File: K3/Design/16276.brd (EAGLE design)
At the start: 40.6 x 52.1 mm, 75 parts, among them J1 PST1,0/4-3,5, J3 PBC03SAA, Q1 K1N, Q10 DMB, Q11 34N, Q12 34N, Q13 K1N, Q14 K1N, Q15 K1N, Q16 K38, Q17 K38, Q18 DMB, Q19 K3N, Q2 DMB, Q20 K3N, Q21 K1N, Q22 DMB, Q23 34N, Q24 K84, Q3 34N, Q4 DMB, Q5 K3N, Q6 K1N, Q7 K1N, Q8 K1N, Q9 K1N, U1 MC34063A, U2 74HC238

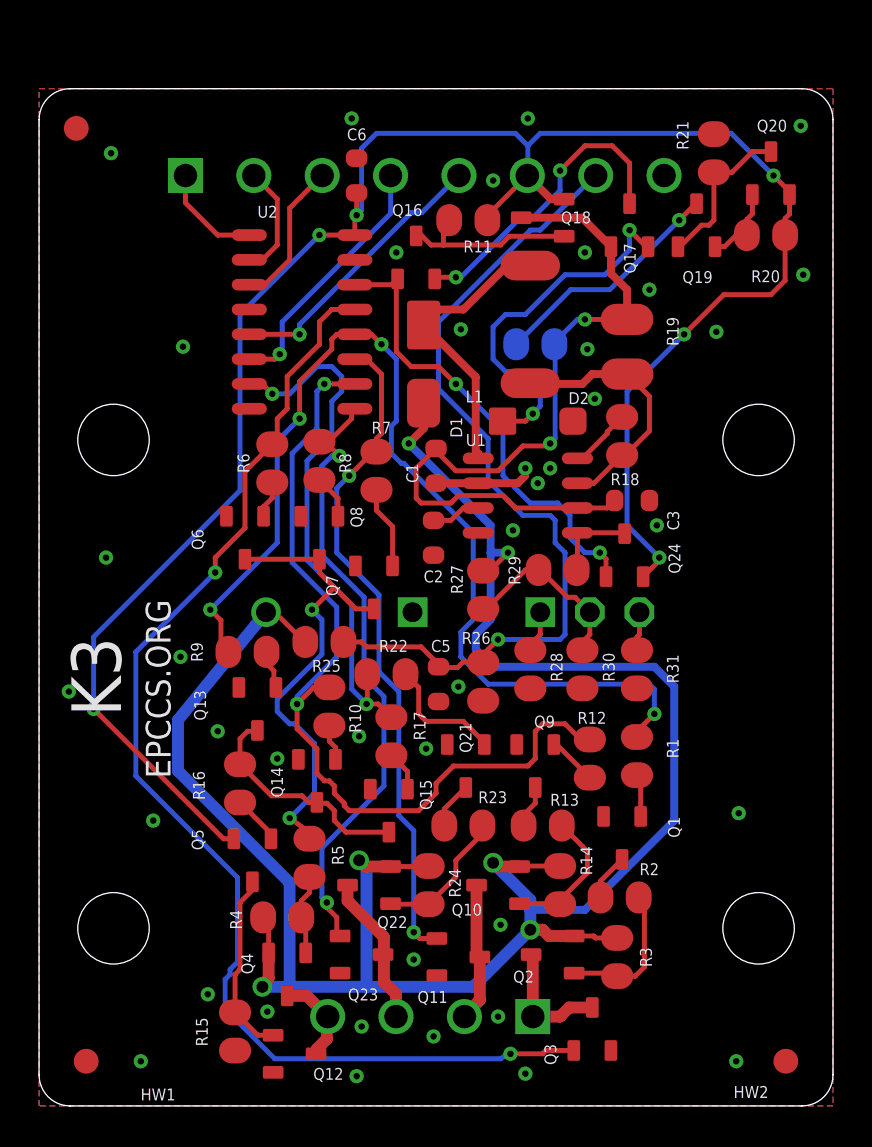
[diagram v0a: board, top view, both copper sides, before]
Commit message: K3: use E3 input to turn on curr source
that test for bridge shorts
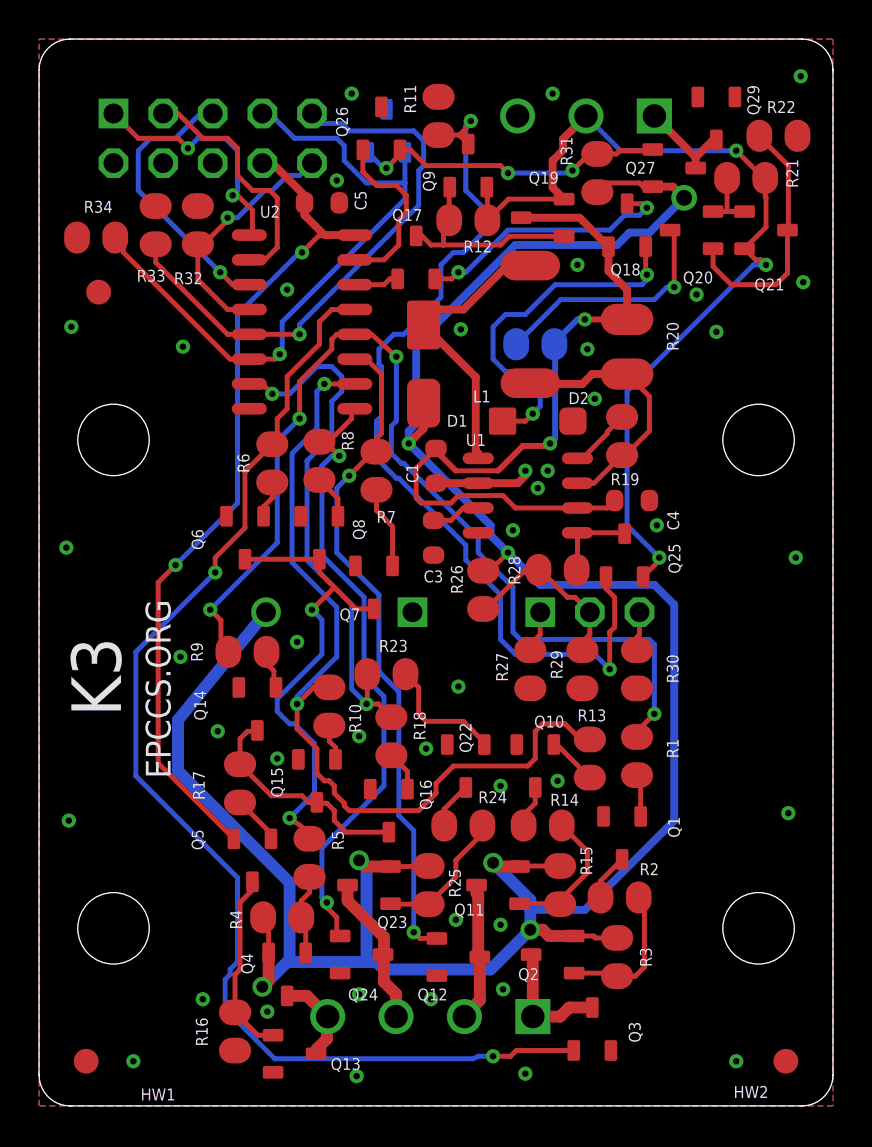
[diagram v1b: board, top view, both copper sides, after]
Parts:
- removed C6: .1uF, C-C:C0603(1608)
- added J4: PBC03SAA, J-HDR2.54mm:1X3
- added Q25: K84, Q-PCH:SOT23
- added Q26: K38, Q-NCH:SOT23
- added Q27: DMB, Q-PCH:SOT23
- added Q28: OPEN, Q-NCH:SOT23
- added Q29: K1N, Q-NPN:SOT23
- added R32, R33, R34: 10K, R-C:C0805(2012)
- added TP1: TPPAD1-08, J-TP:P1-08
- C2: value 330pF -> 2200uF; device C-C:C0603(1608) -> C-Al:E7,5-18
- C3: value .1uF -> 330pF
- C4: value 2200uF -> .1uF; device C-Al:E7,5-18 -> C-C:C0603(1608)
- C5: value .01uF -> .1uF
- J2: value (none) -> PST1,0&3-3,5; device J-HDR3.5mm:MCV8 -> J-HDR3.5mm:MCV3
- J3: value PBC03SAA -> (none); device J-HDR2.54mm:1X3 -> J-HDR2.54mm:2X5
- Q10, Q22: value DMB -> K1N; device Q-PCH:SOT23 -> Q-NPN:SOT23
- Q11, Q23: value 34N -> DMB; device Q-NCH:SOT23 -> Q-PCH:SOT23
- Q13: value K1N -> 34N; device Q-NPN:SOT23 -> Q-NCH:SOT23
- Q16: value K38 -> K1N; device Q-NCH:SOT23 -> Q-NPN:SOT23
- Q18: value DMB -> K38; device Q-PCH:SOT23 -> Q-NCH:SOT23
- Q19: value K3N -> DMB; device Q-PNP:SOT23 -> Q-PCH:SOT23
- Q21: value K1N -> K3N; device Q-NPN:SOT23 -> Q-PNP:SOT23
- Q24: value K84 -> 34N; device Q-PCH:SOT23 -> Q-NCH:SOT23
- Q9: value K1N -> K84; device Q-NPN:SOT23 -> Q-PCH:SOT23
- R11, R22: value 10K -> 49.9k
- R13, R16, R23: value 100K -> 10K
- R15: value 10K -> 100K
- R18: value 182 -> 100K
- R19: value 1 -> 182; device R-C:C1210(3225) -> R-C:C0805(2012)
- R20: value 32.4 -> 1; device R-C:C0805(2012) -> R-C:C1210(3225)
- R21: value 49.9k -> 32.4
- R26: value 5.62K -> 100K
- R27: value 100K -> 15.8k
- R28: value 15.8k -> 10K
- R29: value 10K -> 8.45k
- R30: value 8.45k -> 43.2k
- R31: value 43.2k -> 100K
- moved R22 34.1 mm to (37.8, 49.7), turned to 180 degrees
- moved J3 33.6 mm to (3.81, 50.8)
- moved Q21 31.4 mm to (37.2, 44.8), turned to 270 degrees
- moved Q9 30.9 mm to (22.0, 48.1), turned to 0 degrees
- moved Q16 28.4 mm to (17.9, 15.1), turned to 180 degrees
- moved R12 28.3 mm to (22.0, 45.3), turned to 180 degrees
- moved R31 25.5 mm to (28.6, 47.8), turned to 90 degrees
- moved C5 25.4 mm to (14.5, 46.2), turned to 0 degrees
- moved Q24 24.5 mm to (16.5, 7.75), turned to 270 degrees
- moved J2 24.2 mm to (31.5, 50.7), turned to 0 degrees
- moved R18 19.4 mm to (18.0, 18.9), turned to 270 degrees
- moved R15 18.2 mm to (26.7, 11.3)
- moved Q13 17.8 mm to (13.1, 2.67), turned to 270 degrees
- moved C4 16.0 mm to (30.4, 31.0), flipped to the top, turned to 0 degrees
- moved R25 13.5 mm to (19.9, 11.3), turned to 90 degrees
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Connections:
- removed net !EN: J2.5, U2.5
- removed net +5V: C6.1, J2.6, Q18.2(S), Q20.E, Q24.2(S), Q5.E, R11.1, R20.2, U2.16
- removed net 5.3%BOOST: C5.1, J2.7, R25.2, R26.2
- removed net EN: J2.4, U2.6
- new net !E1: J3.10, R32.1, U2.4
- new net !E2: J3.9, R33.1, U2.5
- new net DISCHARGE: J2.1, Q27.3(D), Q29.C
- new net E3: J3.7, Q28.1(G), R34.1, U2.6
- new net FEED: C1.1, C4.1, D3.K, Q18.1(G), Q19.3(D), R20.1, U1.6
- new net N$10: Q26.2(S), Q27.1(G), Q28.2(S), R31.2
- new net N$11: Q26.1(G), U2.15
- new net N$2: Q25.1(G), Q9.3(D), R11.1
- new net SUPPLY: J2.2, Q19.2(S), Q21.E, Q25.2(S), Q9.2(S), R12.1, R21.2
- net 0V: now also C2.-, C4.2, J2.3, J3.2, J3.4, J3.6, Q10.E, Q13.2(S), Q16.E, Q22.E, Q24.2(S), Q26.3(D), Q28.3(D), Q29.B, Q29.E, R11.2, R16.1, R22.1, R27.1, R29.2, R32.2, R33.2, R34.2; no longer C2.2, C4.-, C6.2, J2.8, Q11.2(S), Q13.E, Q21.E, Q23.2(S), Q9.E, R15.1, R21.1, R26.1, R28.1, R31.2, U2.4
- net A0: now also J3.1; no longer J2.1
- net A1: now also J3.3; no longer J2.2
- net A2: now also J3.5; no longer J2.3
- net BOOST: now also C2.+, Q11.2(S), Q23.2(S), Q27.2(S), R15.2, R25.2, R26.1, R31.1, TP1.TP; no longer C4.+, Q10.2(S), Q22.2(S), R14.2, R24.2, R25.1, R27.1
- net COM: now also Q13.3(D); no longer Q12.3(D)
- net K2: now also Q12.3(D); no longer Q10.3(D)
- net K3: now also Q24.3(D); no longer Q22.3(D)
- net N$120: now also J4.3, R30.1; no longer J3.3, R31.1
- net N$121: now also J4.1, R29.1; no longer J3.1, R30.1
- net N$128: now also Q20.E, Q21.B, R21.1; no longer Q19.E, Q20.B, R20.1
- net N$13: now also R19.2; no longer R18.2
- net N$132: now also Q20.B, Q21.C, R22.2; no longer Q19.B, Q20.C, R21.2
- net N$14: now also R19.1, R20.2; no longer R18.1, R19.2
- net N$16: now also C3.1; no longer C2.1
- net N$21: now also Q13.1(G), R16.2; no longer Q12.1(G), R15.2
- net N$22: now also Q17.3(D), Q19.1(G), Q9.1(G), R12.2; no longer Q16.3(D), Q18.1(G), R11.2
- net N$26: now also J4.2, R26.2, R28.1; no longer J3.2, R28.2, R29.1
- net N$3: now also Q23.1(G), R24.2, R25.1; no longer Q22.1(G), R23.2, R24.1
- net N$4: now also Q22.C, R24.1; no longer Q21.C, R23.1
- net N$43: now also Q11.1(G), R14.2, R15.1; no longer Q10.1(G), R13.2, R14.1
- net N$44: now also Q10.C, R14.1; no longer Q9.C, R13.1
- net N$45: now also Q10.B, R13.2; no longer Q9.B, R12.2
- net N$5: now also Q22.B, R23.2; no longer Q21.B, R22.2
- net N$6: now also Q17.2(S), Q18.3(D); no longer Q16.2(S), Q17.3(D)
- net N$7: now also Q25.3(D), R28.2; no longer Q24.3(D), R29.2
- net N$72: now also R17.2; no longer R16.2
- net N$73: now also Q16.C, R17.1; no longer Q13.C, R16.1
- net N$79: now also Q14.B; no longer Q13.B
- net N$8: now also Q18.2(S); no longer Q17.2(S)
- net N$81: now also Q15.B; no longer Q14.B
- net N$86: now also Q20.C; no longer Q19.C
- net N$87: now also Q16.B, R18.2; no longer Q15.B, R17.2
- net RESET-K2: now also R13.1; no longer R12.1
- net RESET-K3: now also R18.1, R23.1; no longer R17.1, R22.1
- net SET-K2: now also Q12.1(G); no longer Q11.1(G)
- net SET-K3: now also Q24.1(G); no longer Q23.1(G)
- net SMPS: now also Q17.1(G); no longer Q16.1(G), Q24.1(G)
- net VCC: now also C5.1, J3.8, Q5.E, U2.16; no longer C1.1, C3.1, D3.K, Q17.1(G), Q18.3(D), R19.1, U1.6
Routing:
- net +5V: track 103.1 -> 0.00 mm, vias 6 -> 0
- net SUPPLY: track 0.00 -> 47.6 mm, vias 0 -> 3
- net N$2: track 0.00 -> 46.8 mm, vias 0 -> 2
- net 5.3%BOOST: track 43.6 -> 0.00 mm, vias 1 -> 0
- net FEED: track 0.00 -> 39.5 mm, vias 0 -> 2
- net E3: track 0.00 -> 33.5 mm, vias 0 -> 1
- net !E2: track 0.00 -> 28.6 mm, vias 0 -> 1
- net SMPS: track 24.0 -> 2.32 mm, vias 2 -> 0
- net BOOST: track 111.8 -> 131.1 mm
- net N$10: track 0.00 -> 16.4 mm, vias 0 -> 3
- net !EN: track 14.4 -> 0.00 mm, vias 1 -> 0
- net EN: track 13.2 -> 0.00 mm, vias 1 -> 0
- net !E1: track 0.00 -> 12.7 mm, vias 0 -> 1
- net N$11: track 0.00 -> 9.11 mm
- net A0: track 5.35 -> 12.6 mm, vias 0 -> 2
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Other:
- board size 40.6 x 52.1 mm -> 40.6 x 54.6 mm
- board text added: "16276^1"
- board text added: "BOOST OUT"
- board text added: "E3"
- board text added: "SUPPLY"
- board text added: "VCC"
- board text added: "nE1"
- board text added: "nE2"
- board text removed: "!EN"
- board text removed: "16276^0"
- board text removed: "5.3%BOOST"
- board text removed: "5V"
- board text removed: "EN"

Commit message: K3: ^2 review
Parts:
- removed Q27: DMB, Q-PCH:SOT23
- removed Q28: OPEN, Q-NCH:SOT23
- removed Q29: K1N, Q-NPN:SOT23
- R31: value 100K -> JMP
- moved TP1 18.0 mm to (25.7, 30.1)
- moved Q26 17.1 mm to (34.5, 51.4), turned to 270 degrees
- moved R31 3.05 mm to (31.5, 46.9), flipped to the bottom
- moved R22 0.85 mm to (37.5, 50.4), turned to 270 degrees
- moved R11 0.38 mm to (20.4, 51.1)
- moved Q5 0.25 mm to (10.7, 12.6)
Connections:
- removed net DISCHARGE: J2.1, Q27.3(D), Q29.C
- removed net N$10: Q26.2(S), Q27.1(G), Q28.2(S), R31.2
- removed net N$11: Q26.1(G), U2.15
- new net EN17MA: Q26.3(D), R22.1
- net 0V: now also Q26.2(S); no longer Q26.3(D), Q28.3(D), Q29.B, Q29.E, R22.1
- net BOOST: now also J2.1, R31.2; no longer Q27.2(S), TP1.TP
- net E3: now also Q26.1(G); no longer Q28.1(G)
- net FEED: now also TP1.TP
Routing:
- net E3: track 33.5 -> 50.0 mm, vias 1 -> 4
- net N$10: track 16.4 -> 0.00 mm, vias 3 -> 0
- net N$11: track 9.11 -> 0.00 mm
- net DISCHARGE: track 4.97 -> 0.00 mm
- net N$2: track 46.8 -> 43.4 mm
- net !E2: track 28.6 -> 26.5 mm
- net SUPPLY: track 47.6 -> 49.7 mm
- net N$6: track 13.7 -> 11.6 mm
- net EN17MA: track 0.00 -> 1.84 mm
- net N$27: track 25.2 -> 24.4 mm
- net BOOST: track 131.1 -> 130.3 mm
- net FEED: track 39.5 -> 40.0 mm
- net 0V: vias 43 -> 58
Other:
- board text added: "16276^2"
- board text added: "RPUBUS.ORG"
- board text removed: "16276^1"
- board text removed: "EPCCS.ORG"
